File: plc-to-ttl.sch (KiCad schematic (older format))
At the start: 10 parts, among them J1 Screw_Terminal_01x08, J2 Screw_Terminal_01x08

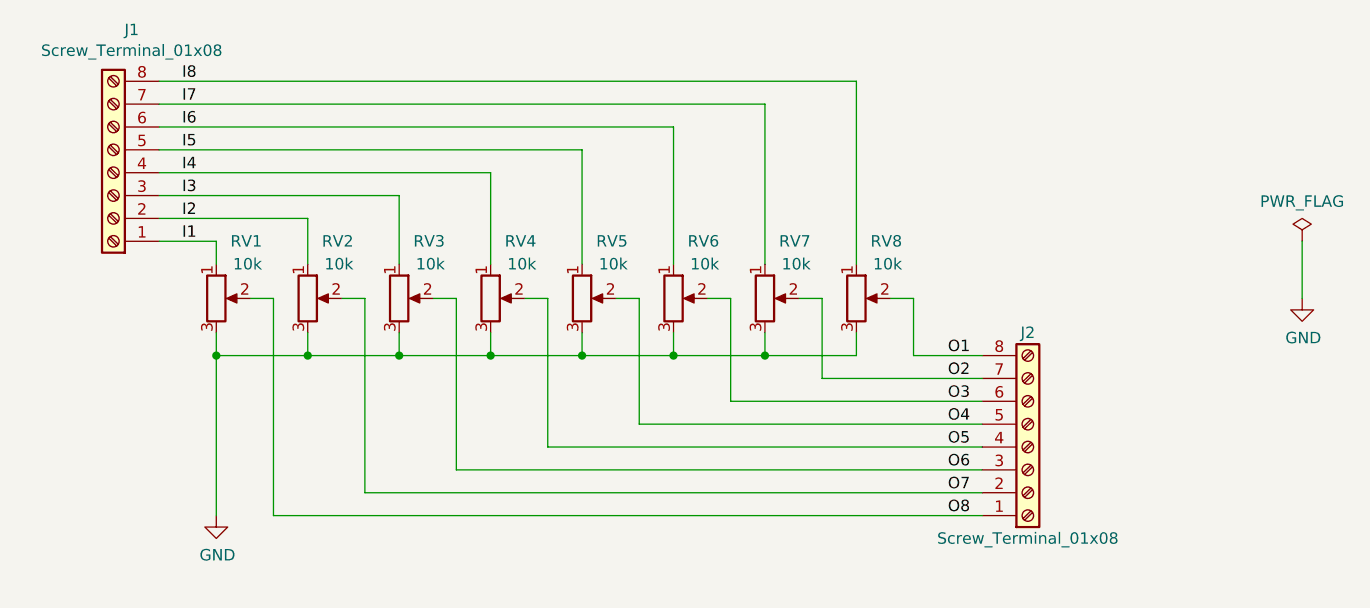
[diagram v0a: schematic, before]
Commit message: Reorganized everything to use hierarchical sheets in KiCAD. Moved power supply section for motor driver into separate sheet. Moved connectors into top-level sheet
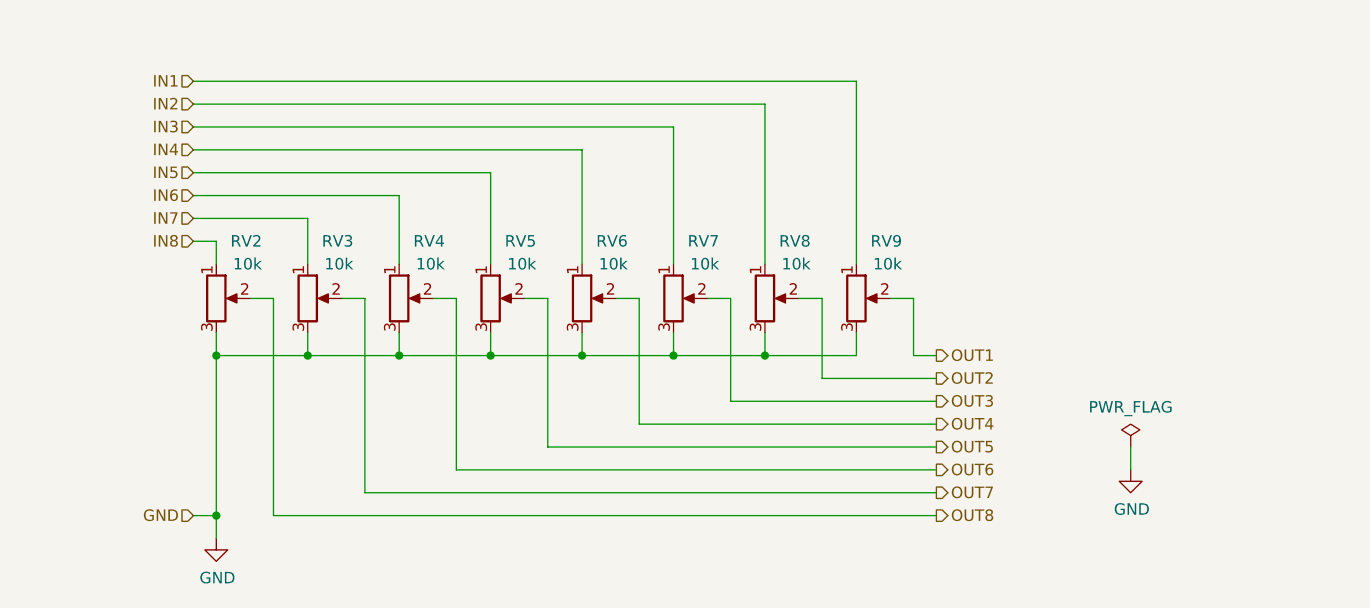
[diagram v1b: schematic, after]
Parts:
- removed J1, J2: Screw_Terminal_01x08, TerminalBlock_RND:TerminalBlock_RND_205-00282_1x08_P5.00mm_Vertical, symbol Connector:Screw_Terminal_01x08
- renumbered RV1 to RV2, RV2 to RV3, RV3 to RV4, RV4 to RV5, RV5 to RV6, RV6 to RV7, RV7 to RV8, RV8 to RV9
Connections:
- net I1 renamed IN8
- net I2 renamed IN7
- net I3 renamed IN6
- net I4 renamed IN5
- net I5 renamed IN4
- net I6 renamed IN3
- net I7 renamed IN2
- net I8 renamed IN1
- net O1 renamed OUT1
- net O2 renamed OUT2
- net O3 renamed OUT3
- net O4 renamed OUT4
- net O5 renamed OUT5
- net O6 renamed OUT6
- net O7 renamed OUT7
- net O8 renamed OUT8
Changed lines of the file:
@@
 EESchema Schematic File Version 4
-LIBS:plc-to-ttl-cache
+LIBS:plc-utility-board-cache
 EELAYER 26 0
 EELAYER END
 $Descr A4 11693 8268
 encoding utf-8
-Sheet 1 1
+Sheet 10 10
 Title ""
 Date ""
@@
 $EndDescr
 $Comp
-L Connector:Screw_Terminal_01x08 J1
-U 1 1 5BD3FE4D
-P 3800 2900
-F 0 "J1" H 3720 2275 50  0000 C CNN
-F 1 "Screw_Terminal_01x08" H 3720 2366 50  0000 C CNN
-F 2 "TerminalBlock_RND:TerminalBlock_RND_205-00282_1x08_P5.00mm_Vertical" H 3800 2900 50  0001 C CNN
-F 3 "~" H 3800 2900 50  0001 C CNN
-	1    3800 2900
-	-1   0    0    1
-$EndComp
-$Comp
-L Device:R_POT RV1
+L Device:R_POT RV2
 U 1 1 5BD40A2B
 P 4250 3450
-F 0 "RV1" H 4450 3700 50  0000 R CNN
+AR Path="/5BDB568B/5BD40A2B" Ref="RV2"  Part="1"
+AR Path="/5BEFAA7D/5BD40A2B" Ref="RV?"  Part="1"
+AR Path="/5BEFD0FF/5BD40A2B" Ref="RV?"  Part="1"
+F 0 "RV2" H 4450 3700 50  0000 R CNN
 F 1 "10k" H 4450 3600 50  0000 R CNN
 F 2 "Potentiometer_THT:Potentiometer_Bourns_3266W_Vertical" H 4250 3450 50  0001 C CNN
@@
 $EndComp
 $Comp
-L Connector:Screw_Terminal_01x08 J2
-U 1 1 5BD40CFF
-P 7800 4100
-F 0 "J2" H 7800 3600 50  0000 C CNN
-F 1 "Screw_Terminal_01x08" H 7800 4500 50  0000 C CNN
-F 2 "TerminalBlock_RND:TerminalBlock_RND_205-00282_1x08_P5.00mm_Vertical" H 7800 4100 50  0001 C CNN
-F 3 "~" H 7800 4100 50  0001 C CNN
-	1    7800 4100
-	1    0    0    1
-$EndComp
-$Comp
-L Device:R_POT RV2
+L Device:R_POT RV3
 U 1 1 5BD4124B
 P 4650 3450
-F 0 "RV2" H 4850 3700 50  0000 R CNN
+AR Path="/5BDB568B/5BD4124B" Ref="RV3"  Part="1"
+AR Path="/5BEFAA7D/5BD4124B" Ref="RV?"  Part="1"
+AR Path="/5BEFD0FF/5BD4124B" Ref="RV?"  Part="1"
+F 0 "RV3" H 4850 3700 50  0000 R CNN
 F 1 "10k" H 4850 3600 50  0000 R CNN
 F 2 "Potentiometer_THT:Potentiometer_Bourns_3266W_Vertical" H 4650 3450 50  0001 C CNN
@@
 	1    0    0    -1
 $EndComp
-$Comp
-L power:GND #PWR01
-U 1 1 5BD413CC
-P 4250 4400
-F 0 "#PWR01" H 4250 4150 50  0001 C CNN
-F 1 "GND" H 4255 4227 50  0000 C CNN
-F 2 "" H 4250 4400 50  0001 C CNN
-F 3 "" H 4250 4400 50  0001 C CNN
-	1    4250 4400
-	1    0    0    -1
-$EndComp
-Wire Wire Line
-	4250 4400 4250 3700
 Wire Wire Line
 	4250 3700 4650 3700
@@
 	4250 3700 4250 3600
 $Comp
-L Device:R_POT RV3
+L Device:R_POT RV4
 U 1 1 5BD41463
 P 5050 3450
-F 0 "RV3" H 5250 3700 50  0000 R CNN
+AR Path="/5BDB568B/5BD41463" Ref="RV4"  Part="1"
+AR Path="/5BEFAA7D/5BD41463" Ref="RV?"  Part="1"
+AR Path="/5BEFD0FF/5BD41463" Ref="RV?"  Part="1"
+F 0 "RV4" H 5250 3700 50  0000 R CNN
 F 1 "10k" H 5250 3600 50  0000 R CNN
 F 2 "Potentiometer_THT:Potentiometer_Bourns_3266W_Vertical" H 5050 3450 50  0001 C CNN
@@
 Connection ~ 4650 3700
 $Comp
-L Device:R_POT RV4
+L Device:R_POT RV5
 U 1 1 5BD414F9
 P 5450 3450
-F 0 "RV4" H 5650 3700 50  0000 R CNN
+AR Path="/5BDB568B/5BD414F9" Ref="RV5"  Part="1"
+AR Path="/5BEFAA7D/5BD414F9" Ref="RV?"  Part="1"
+AR Path="/5BEFD0FF/5BD414F9" Ref="RV?"  Part="1"
+F 0 "RV5" H 5650 3700 50  0000 R CNN
 F 1 "10k" H 5650 3600 50  0000 R CNN
 F 2 "Potentiometer_THT:Potentiometer_Bourns_3266W_Vertical" H 5450 3450 50  0001 C CNN
@@
 	4500 3450 4500 4400
 Wire Wire Line
-	4500 4400 7600 4400
+	4500 4400 7400 4400
 Wire Wire Line
 	4800 3450 4900 3450
@@
 	4900 3450 4900 4300
 Wire Wire Line
-	4900 4300 7600 4300
+	4900 4300 7400 4300
 Wire Wire Line
 	5200 3450 5300 3450
@@
 	5300 3450 5300 4200
 Wire Wire Line
-	5300 4200 7600 4200
+	5300 4200 7400 4200
 Wire Wire Line
 	5600 3450 5700 3450
@@
 	5700 3450 5700 4100
 Wire Wire Line
-	5700 4100 7600 4100
-$Comp
-L Device:R_POT RV5
+	5700 4100 7400 4100
+$Comp
+L Device:R_POT RV6
 U 1 1 5BD46C30
 P 5850 3450
-F 0 "RV5" H 6050 3700 50  0000 R CNN
+AR Path="/5BDB568B/5BD46C30" Ref="RV6"  Part="1"
+AR Path="/5BEFAA7D/5BD46C30" Ref="RV?"  Part="1"
+AR Path="/5BEFD0FF/5BD46C30" Ref="RV?"  Part="1"
+F 0 "RV6" H 6050 3700 50  0000 R CNN
 F 1 "10k" H 6050 3600 50  0000 R CNN
 F 2 "Potentiometer_THT:Potentiometer_Bourns_3266W_Vertical" H 5850 3450 50  0001 C CNN
@@
 	6100 3450 6100 4000
 Wire Wire Line
-	6100 4000 7600 4000
+	6100 4000 7400 4000
 Wire Wire Line
 	5450 3700 5850 3700
@@
 	5850 2800 5850 3300
 $Comp
-L Device:R_POT RV6
+L Device:R_POT RV7
 U 1 1 5BD4810A
 P 6250 3450
-F 0 "RV6" H 6450 3700 50  0000 R CNN
+AR Path="/5BDB568B/5BD4810A" Ref="RV7"  Part="1"
+AR Path="/5BEFAA7D/5BD4810A" Ref="RV?"  Part="1"
+AR Path="/5BEFD0FF/5BD4810A" Ref="RV?"  Part="1"
+F 0 "RV7" H 6450 3700 50  0000 R CNN
 F 1 "10k" H 6450 3600 50  0000 R CNN
 F 2 "Potentiometer_THT:Potentiometer_Bourns_3266W_Vertical" H 6250 3450 50  0001 C CNN
@@
 	6500 3450 6500 3900
 Wire Wire Line
-	6500 3900 7600 3900
+	6500 3900 7400 3900
 Wire Wire Line
 	5850 3700 6250 3700
@@
 Connection ~ 5850 3700
 $Comp
-L Device:R_POT RV7
+L Device:R_POT RV8
 U 1 1 5BD4A795
 P 6650 3450
-F 0 "RV7" H 6850 3700 50  0000 R CNN
+AR Path="/5BDB568B/5BD4A795" Ref="RV8"  Part="1"
+AR Path="/5BEFAA7D/5BD4A795" Ref="RV?"  Part="1"
+AR Path="/5BEFD0FF/5BD4A795" Ref="RV?"  Part="1"
+F 0 "RV8" H 6850 3700 50  0000 R CNN
 F 1 "10k" H 6850 3600 50  0000 R CNN
 F 2 "Potentiometer_THT:Potentiometer_Bourns_3266W_Vertical" H 6650 3450 50  0001 C CNN
@@
 	6900 3450 6900 3800
 Wire Wire Line
-	6900 3800 7600 3800
-$Comp
-L Device:R_POT RV8
+	6900 3800 7400 3800
+$Comp
+L Device:R_POT RV9
 U 1 1 5BD4C495
 P 7050 3450
-F 0 "RV8" H 7250 3700 50  0000 R CNN
+AR Path="/5BDB568B/5BD4C495" Ref="RV9"  Part="1"
+AR Path="/5BEFAA7D/5BD4C495" Ref="RV?"  Part="1"
+AR Path="/5BEFD0FF/5BD4C495" Ref="RV?"  Part="1"
+F 0 "RV9" H 7250 3700 50  0000 R CNN
 F 1 "10k" H 7250 3600 50  0000 R CNN
 F 2 "Potentiometer_THT:Potentiometer_Bourns_3266W_Vertical" H 7050 3450 50  0001 C CNN
@@
 	7300 3450 7300 3700
 Wire Wire Line
-	7300 3700 7600 3700
+	7300 3700 7400 3700
 Wire Wire Line
 	6650 3700 7050 3700
@@
 Wire Wire Line
 	7050 3300 7050 2500
-Text Label 4100 2500 0    50   ~ 0
-I8
-Text Label 4100 2600 0    50   ~ 0
-I7
-Text Label 4100 2700 0    50   ~ 0
-I6
-Text Label 4100 2800 0    50   ~ 0
-I5
-Text Label 4100 2900 0    50   ~ 0
-I4
-Text Label 4100 3000 0    50   ~ 0
-I3
-Text Label 4100 3100 0    50   ~ 0
-I2
-Text Label 4100 3200 0    50   ~ 0
-I1
-Wire Wire Line
-	4000 3200 4250 3200
-Wire Wire Line
-	4000 3100 4650 3100
-Wire Wire Line
-	4000 3000 5050 3000
-Wire Wire Line
-	4000 2900 5450 2900
-Wire Wire Line
-	4000 2800 5850 2800
-Wire Wire Line
-	4000 2700 6250 2700
-Wire Wire Line
-	4000 2600 6650 2600
-Wire Wire Line
-	4000 2500 7050 2500
-Text Label 7450 4400 0    50   ~ 0
-O8
-Text Label 7450 4300 0    50   ~ 0
-O7
-Text Label 7450 4200 0    50   ~ 0
-O6
-Text Label 7450 4100 0    50   ~ 0
-O5
-Text Label 7450 4000 0    50   ~ 0
-O4
-Text Label 7450 3900 0    50   ~ 0
-O3
-Text Label 7450 3800 0    50   ~ 0
-O2
-Text Label 7450 3700 0    50   ~ 0
-O1
-$Comp
-L power:GND #PWR0101
-U 1 1 5BD2D548
-P 9000 3450
-F 0 "#PWR0101" H 9000 3200 50  0001 C CNN
-F 1 "GND" H 9005 3277 50  0000 C CNN
-F 2 "" H 9000 3450 50  0001 C CNN
-F 3 "" H 9000 3450 50  0001 C CNN
-	1    9000 3450
-	1    0    0    -1
-$EndComp
-$Comp
-L power:PWR_FLAG #FLG0101
-U 1 1 5BD2E284
-P 9000 3200
-F 0 "#FLG0101" H 9000 3275 50  0001 C CNN
-F 1 "PWR_FLAG" H 9000 3374 50  0000 C CNN
-F 2 "" H 9000 3200 50  0001 C CNN
-F 3 "~" H 9000 3200 50  0001 C CNN
-	1    9000 3200
-	1    0    0    -1
-$EndComp
-Wire Wire Line
-	9000 3450 9000 3200
+Wire Wire Line
+	4150 3200 4250 3200
+Wire Wire Line
+	4150 3100 4650 3100
+Wire Wire Line
+	4150 3000 5050 3000
+Wire Wire Line
+	4150 2900 5450 2900
+Wire Wire Line
+	4150 2800 5850 2800
+Wire Wire Line
+	4150 2700 6250 2700
+Wire Wire Line
+	4150 2600 6650 2600
+Wire Wire Line
+	4150 2500 7050 2500
+Text HLabel 4150 4400 0    50   Input ~ 0
+GND
+Text HLabel 4150 2500 0    50   Input ~ 0
+IN1
+Text HLabel 4150 2600 0    50   Input ~ 0
+IN2
+Text HLabel 4150 2700 0    50   Input ~ 0
+IN3
+Text HLabel 4150 2800 0    50   Input ~ 0
+IN4
+Text HLabel 4150 2900 0    50   Input ~ 0
+IN5
+Text HLabel 4150 3000 0    50   Input ~ 0
+IN6
+Text HLabel 4150 3100 0    50   Input ~ 0
+IN7
+Text HLabel 4150 3200 0    50   Input ~ 0
+IN8
+Text HLabel 7400 3700 2    50   Output ~ 0
+OUT1
+Text HLabel 7400 3800 2    50   Output ~ 0
+OUT2
+Text HLabel 7400 3900 2    50   Output ~ 0
+OUT3
+Text HLabel 7400 4000 2    50   Output ~ 0
+OUT4
+Text HLabel 7400 4100 2    50   Output ~ 0
+OUT5
+Text HLabel 7400 4200 2    50   Output ~ 0
+OUT6
+Text HLabel 7400 4300 2    50   Output ~ 0
+OUT7
+Text HLabel 7400 4400 2    50   Output ~ 0
+OUT8
+Wire Wire Line
+	4250 3700 4250 4400
+Wire Wire Line
+	4250 4400 4150 4400
+$Comp
+L power:GND #PWR014
+U 1 1 5BF5A689
+P 4250 4500
+F 0 "#PWR014" H 4250 4250 50  0001 C CNN
+F 1 "GND" H 4255 4327 50  0000 C CNN
+F 2 "" H 4250 4500 50  0001 C CNN
+F 3 "" H 4250 4500 50  0001 C CNN
+	1    4250 4500
+	1    0    0    -1
+$EndComp
+Wire Wire Line
+	4250 4400 4250 4500
+Connection ~ 4250 4400
+$Comp
+L power:PWR_FLAG #FLG01
+U 1 1 5C0564BD
+P 8250 4100
+F 0 "#FLG01" H 8250 4175 50  0001 C CNN
+F 1 "PWR_FLAG" H 8250 4274 50  0000 C CNN
+F 2 "" H 8250 4100 50  0001 C CNN
+F 3 "~" H 8250 4100 50  0001 C CNN
+	1    8250 4100
+	1    0    0    -1
+$EndComp
+$Comp
+L power:GND #PWR015
+U 1 1 5C056536
+P 8250 4200
+F 0 "#PWR015" H 8250 3950 50  0001 C CNN
+F 1 "GND" H 8255 4027 50  0000 C CNN
+F 2 "" H 8250 4200 50  0001 C CNN
+F 3 "" H 8250 4200 50  0001 C CNN
+	1    8250 4200
+	1    0    0    -1
+$EndComp
+Wire Wire Line
+	8250 4100 8250 4200
 $EndSCHEMATC

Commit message: Generated annotations, netlists and assigned footprints into components
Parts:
- RV2, RV3, RV4, RV5, RV6, RV7, RV8, RV9: footprint Potentiometer_THT:Potentiometer_Bourns_3266W_Vertical -> Potentiometer_THT:Potentiometer_Bourns_3296Y_Vertical
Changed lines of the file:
@@
 F 0 "RV2" H 4450 3700 50  0000 R CNN
 F 1 "10k" H 4450 3600 50  0000 R CNN
-F 2 "Potentiometer_THT:Potentiometer_Bourns_3266W_Vertical" H 4250 3450 50  0001 C CNN
+F 2 "Potentiometer_THT:Potentiometer_Bourns_3296Y_Vertical" H 4250 3450 50  0001 C CNN
 F 3 "~" H 4250 3450 50  0001 C CNN
 	1    4250 3450
@@
 F 0 "RV3" H 4850 3700 50  0000 R CNN
 F 1 "10k" H 4850 3600 50  0000 R CNN
-F 2 "Potentiometer_THT:Potentiometer_Bourns_3266W_Vertical" H 4650 3450 50  0001 C CNN
+F 2 "Potentiometer_THT:Potentiometer_Bourns_3296Y_Vertical" H 4650 3450 50  0001 C CNN
 F 3 "~" H 4650 3450 50  0001 C CNN
 	1    4650 3450
@@
 F 0 "RV4" H 5250 3700 50  0000 R CNN
 F 1 "10k" H 5250 3600 50  0000 R CNN
-F 2 "Potentiometer_THT:Potentiometer_Bourns_3266W_Vertical" H 5050 3450 50  0001 C CNN
+F 2 "Potentiometer_THT:Potentiometer_Bourns_3296Y_Vertical" H 5050 3450 50  0001 C CNN
 F 3 "~" H 5050 3450 50  0001 C CNN
 	1    5050 3450
@@
 F 0 "RV5" H 5650 3700 50  0000 R CNN
 F 1 "10k" H 5650 3600 50  0000 R CNN
-F 2 "Potentiometer_THT:Potentiometer_Bourns_3266W_Vertical" H 5450 3450 50  0001 C CNN
+F 2 "Potentiometer_THT:Potentiometer_Bourns_3296Y_Vertical" H 5450 3450 50  0001 C CNN
 F 3 "~" H 5450 3450 50  0001 C CNN
 	1    5450 3450
@@
 F 0 "RV6" H 6050 3700 50  0000 R CNN
 F 1 "10k" H 6050 3600 50  0000 R CNN
-F 2 "Potentiometer_THT:Potentiometer_Bourns_3266W_Vertical" H 5850 3450 50  0001 C CNN
+F 2 "Potentiometer_THT:Potentiometer_Bourns_3296Y_Vertical" H 5850 3450 50  0001 C CNN
 F 3 "~" H 5850 3450 50  0001 C CNN
 	1    5850 3450
@@
 F 0 "RV7" H 6450 3700 50  0000 R CNN
 F 1 "10k" H 6450 3600 50  0000 R CNN
-F 2 "Potentiometer_THT:Potentiometer_Bourns_3266W_Vertical" H 6250 3450 50  0001 C CNN
+F 2 "Potentiometer_THT:Potentiometer_Bourns_3296Y_Vertical" H 6250 3450 50  0001 C CNN
 F 3 "~" H 6250 3450 50  0001 C CNN
 	1    6250 3450
@@
 F 0 "RV8" H 6850 3700 50  0000 R CNN
 F 1 "10k" H 6850 3600 50  0000 R CNN
-F 2 "Potentiometer_THT:Potentiometer_Bourns_3266W_Vertical" H 6650 3450 50  0001 C CNN
+F 2 "Potentiometer_THT:Potentiometer_Bourns_3296Y_Vertical" H 6650 3450 50  0001 C CNN
 F 3 "~" H 6650 3450 50  0001 C CNN
 	1    6650 3450
@@
 F 0 "RV9" H 7250 3700 50  0000 R CNN
 F 1 "10k" H 7250 3600 50  0000 R CNN
-F 2 "Potentiometer_THT:Potentiometer_Bourns_3266W_Vertical" H 7050 3450 50  0001 C CNN
+F 2 "Potentiometer_THT:Potentiometer_Bourns_3296Y_Vertical" H 7050 3450 50  0001 C CNN
 F 3 "~" H 7050 3450 50  0001 C CNN
 	1    7050 3450
